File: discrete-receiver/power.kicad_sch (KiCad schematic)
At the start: 48 parts, among them J2 Optional 5V DC Jack, U11 Ag9905LP, U13 LM66100DCK, U14 LM66100DCK, U15 LM66100DCK

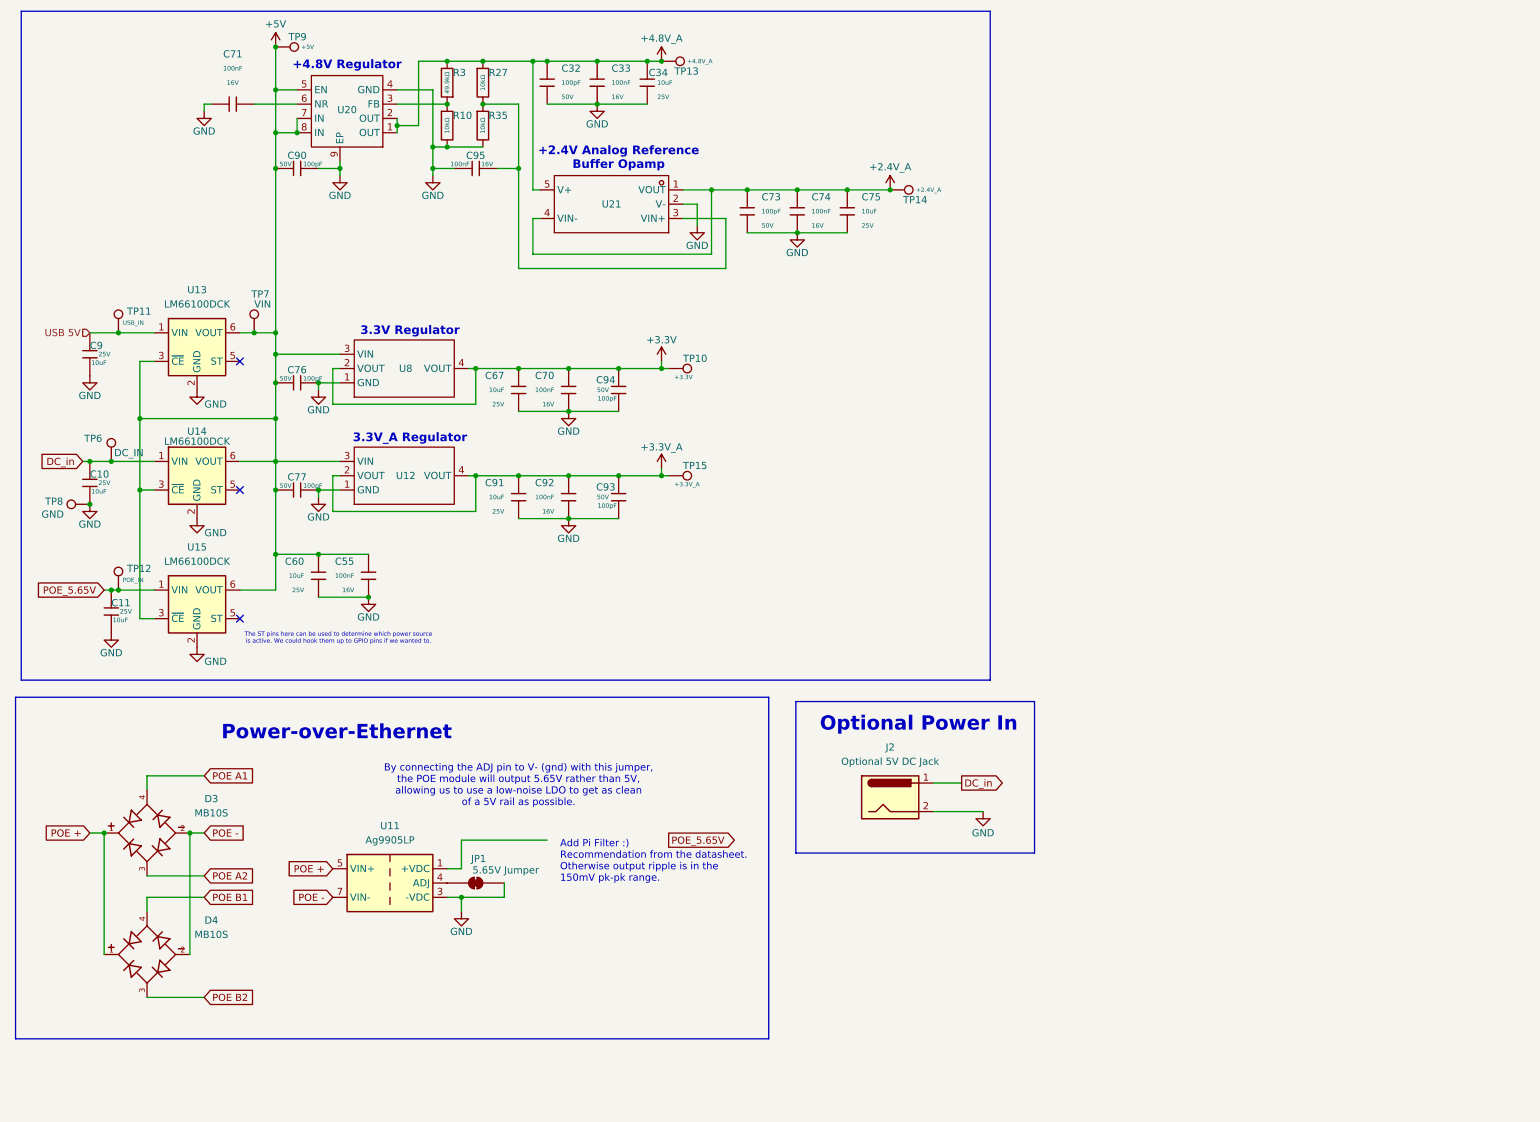
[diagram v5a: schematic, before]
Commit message: Improved POE power filtering and added test points
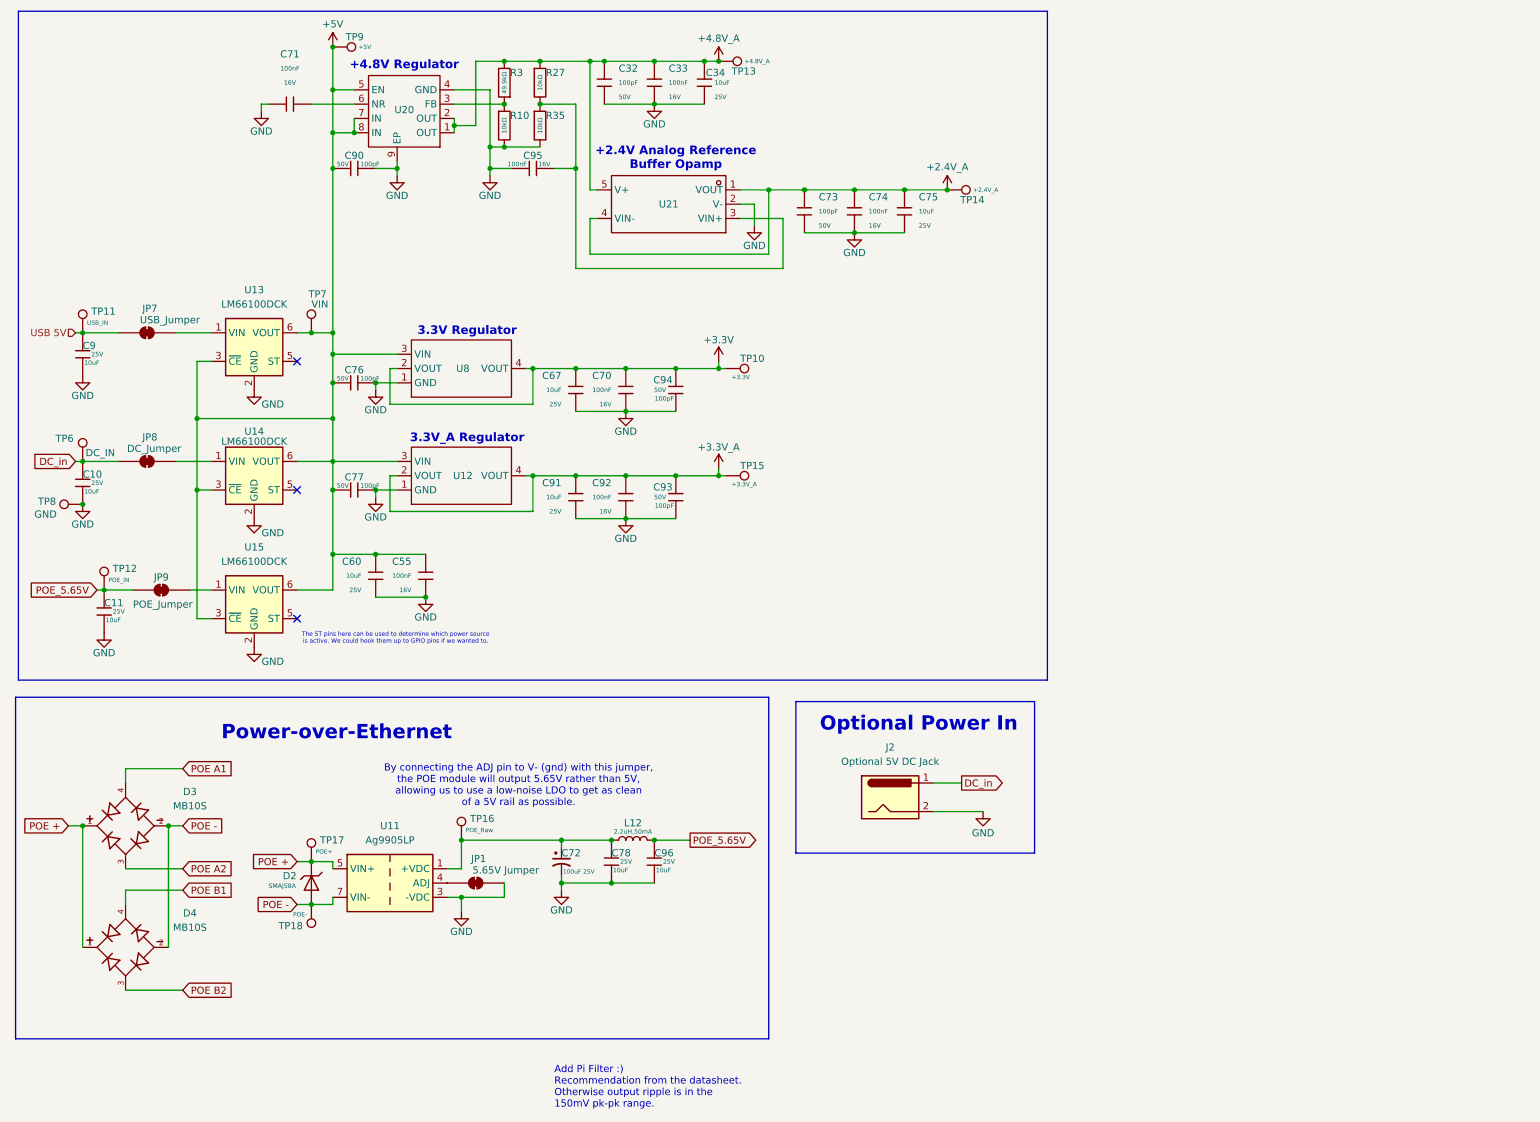
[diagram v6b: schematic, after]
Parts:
- added C72: 100uF 25V, symbol Device:C_Polarized_Small_US
- added C78, C96: 10uF, PCM_JLCPCB:C_0603, symbol PCM_JLCPCB-Capacitors:0603,10uF,(2)
- added D2: SMAJ58A, PCM_JLCPCB:D_DO-214AC(SMA), symbol PCM_JLCPCB-Diodes:TVS-Uni,SMAJ58A
- added JP7: USB_Jumper, symbol Jumper:SolderJumper_2_Bridged
- added JP8: DC_Jumper, symbol Jumper:SolderJumper_2_Bridged
- added JP9: POE_Jumper, symbol Jumper:SolderJumper_2_Bridged
- added L12: 2.2uH,50mA, PCM_JLCPCB:L_0805, symbol PCM_JLCPCB-Inductors:2.2uH,50mA
- added TP16: POE_Raw, symbol Connector:TestPoint
- added TP17: POE+, symbol Connector:TestPoint
- added TP18: POE-, symbol Connector:TestPoint
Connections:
- net DC_in: now also JP8.2 (B); no longer U14.1 (VIN)
- net GND: now also C72.2, C78.2, C96.2
- net POE +: now also D2.1, TP17.1
- net POE -: now also D2.2, TP18.1
- net POE_5.65V: now also C96.1, JP9.2 (B), L12.2; no longer U15.1 (VIN)
- net USB 5V: now also JP7.2 (B); no longer U13.1 (VIN)
- net at U11.1 (+VDC), U11.2 (+VDC): now also C72.1, C78.1, L12.1, TP16.1
- new net: JP8.1 (A), U14.1 (VIN)
- new net: JP9.1 (A), U15.1 (VIN)
- new net: JP7.1 (A), U13.1 (VIN)
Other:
- moved on the sheet: C10, C11, C32, C33, C34, C55, C60, C67, C70, C71, C73, C74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
